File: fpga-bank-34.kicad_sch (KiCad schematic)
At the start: 5 parts, among them U1 XC7K410T-2FFG900I

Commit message: Bump revision to 1.0.0. Update name on schematic and PCB sheets
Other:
- title: K410T devboard -> Kintex 410T devboard

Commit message: Updated libraries for 100nF cap
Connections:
- net +0V675_VREF: now also C375.1
- net GND: now also C375.2
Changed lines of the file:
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@@
       (effects (font (size 1.27 1.27)) (justify left))
     )
+    (pin "1")
+    (pin "2")
   )
   (symbol (lib_id "K410T-devboard:C_100n_0402_EIA") (at 171.45 118.745 0) (unit 1)

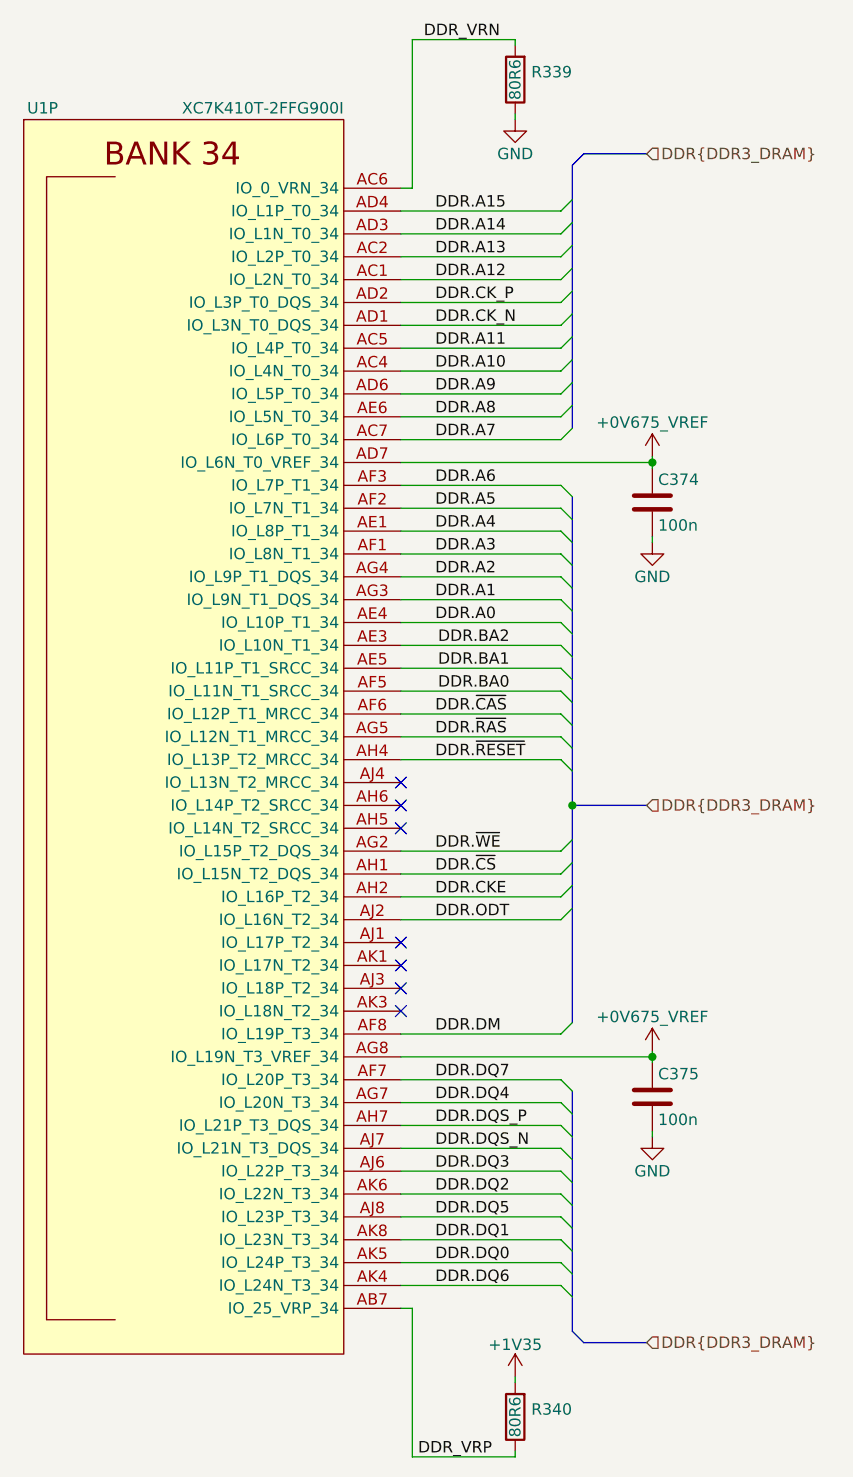
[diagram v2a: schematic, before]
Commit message: Introduce component standardization
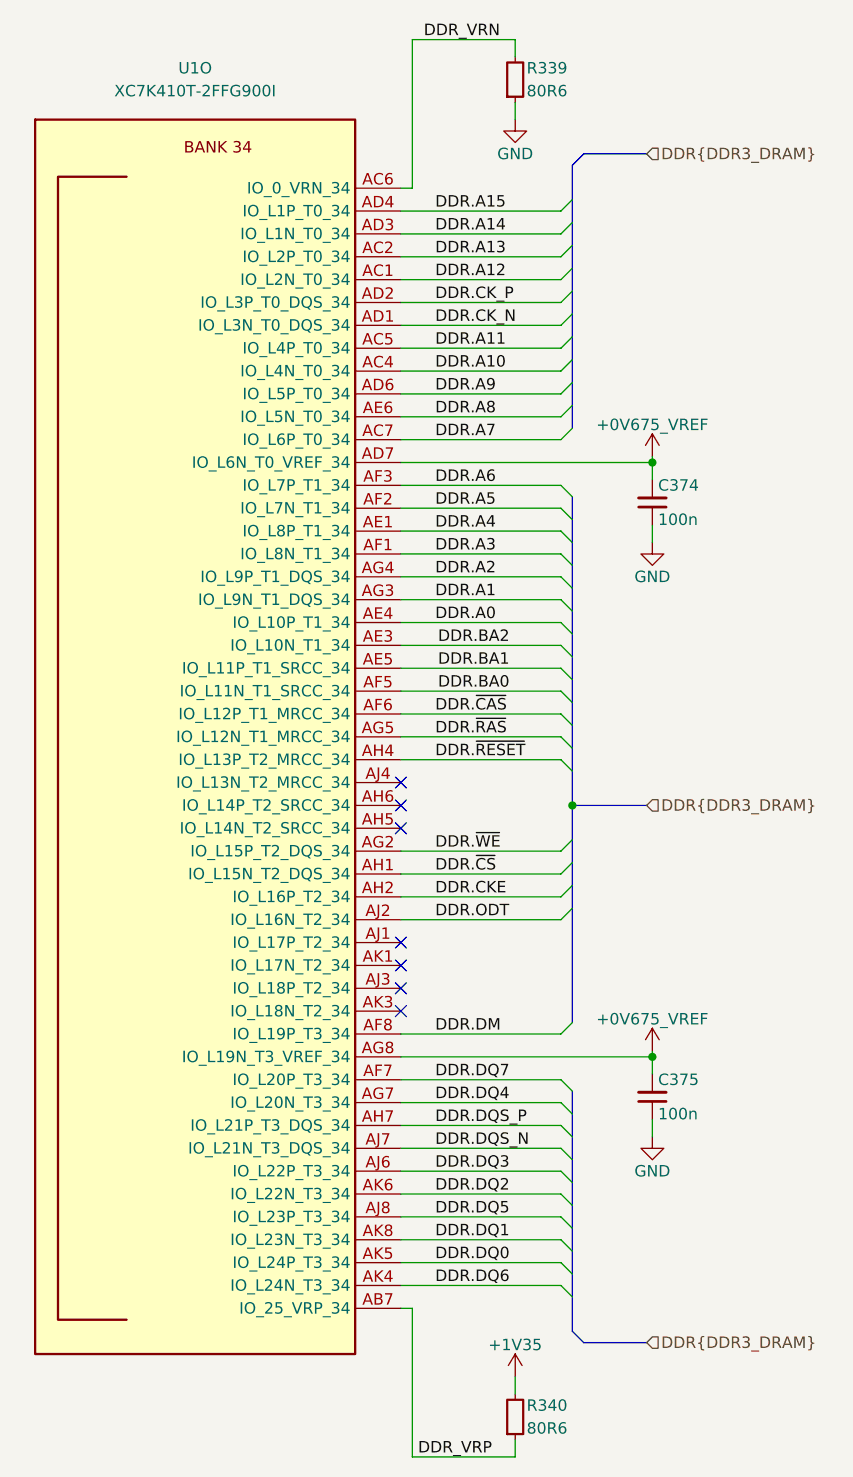
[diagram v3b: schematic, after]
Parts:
- removed U1: XC7K410T-2FFG900I, K410T-devboard-footprints:xc7k410t-2ffg900I, symbol K410T-devboard:XC7K410T-2FFG900I
- added U1: XC7K410T-2FFG900I, K410T-devboard-footprints:xc7k410t-2ffg900I, symbol K410T-devboard:XC7K410T-2FFG900I
- C374, C375: footprint K410T-devboard-footprints:0402-cap_EIA -> K410T-devboard-footprints:C_0402_1005Metric_EIA; Author (none) -> Antmicro; License (none) -> Apache-2.0
- R339, R340: footprint K410T-devboard-footprints:0402-res_EIA -> K410T-devboard-footprints:R_0402_1005Metric_EIA; Author (none) -> Antmicro; License (none) -> Apache-2.0; MPN MC00625W0402180R6 -> CR0402-FX-80R6GLF; Manufacturer MULTICOMP -> Bourns; Tolerance (none) -> 1%
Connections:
- net +0V675_VREF: now also C374.2, C375.2, U1.AD7 (IO_L6N_T0_VREF_34), U1.AG8 (IO_L19N_T3_VREF_34); no longer C374.1, C375.1
- net DDR.A0: now also U1.AE4 (IO_L10P_T1_34)
- net DDR.A1: now also U1.AG3 (IO_L9N_T1_DQS_34)
- net DDR.A10: now also U1.AC4 (IO_L4N_T0_34)
- net DDR.A11: now also U1.AC5 (IO_L4P_T0_34)
- net DDR.A12: now also U1.AC1 (IO_L2N_T0_34)
- net DDR.A13: now also U1.AC2 (IO_L2P_T0_34)
- net DDR.A14: now also U1.AD3 (IO_L1N_T0_34)
- net DDR.A15: now also U1.AD4 (IO_L1P_T0_34)
- net DDR.A2: now also U1.AG4 (IO_L9P_T1_DQS_34)
- net DDR.A3: now also U1.AF1 (IO_L8N_T1_34)
- net DDR.A4: now also U1.AE1 (IO_L8P_T1_34)
- net DDR.A5: now also U1.AF2 (IO_L7N_T1_34)
- net DDR.A6: now also U1.AF3 (IO_L7P_T1_34)
- net DDR.A7: now also U1.AC7 (IO_L6P_T0_34)
- net DDR.A8: now also U1.AE6 (IO_L5N_T0_34)
- net DDR.A9: now also U1.AD6 (IO_L5P_T0_34)
- net DDR.BA0: now also U1.AF5 (IO_L11N_T1_SRCC_34)
- net DDR.BA1: now also U1.AE5 (IO_L11P_T1_SRCC_34)
- net DDR.BA2: now also U1.AE3 (IO_L10N_T1_34)
- net DDR.CKE: now also U1.AH2 (IO_L16P_T2_34)
- net DDR.CK_N: now also U1.AD1 (IO_L3N_T0_DQS_34)
- net DDR.CK_P: now also U1.AD2 (IO_L3P_T0_DQS_34)
- net DDR.DM: now also U1.AF8 (IO_L19P_T3_34)
- net DDR.DQ0: now also U1.AK5 (IO_L24P_T3_34)
- net DDR.DQ1: now also U1.AK8 (IO_L23N_T3_34)
- net DDR.DQ2: now also U1.AK6 (IO_L22N_T3_34)
- net DDR.DQ3: now also U1.AJ6 (IO_L22P_T3_34)
- net DDR.DQ4: now also U1.AG7 (IO_L20N_T3_34)
- net DDR.DQ5: now also U1.AJ8 (IO_L23P_T3_34)
- net DDR.DQ6: now also U1.AK4 (IO_L24N_T3_34)
- net DDR.DQ7: now also U1.AF7 (IO_L20P_T3_34)
- net DDR.DQS_N: now also U1.AJ7 (IO_L21N_T3_DQS_34)
- net DDR.DQS_P: now also U1.AH7 (IO_L21P_T3_DQS_34)
- net DDR.ODT: now also U1.AJ2 (IO_L16N_T2_34)
- net DDR.~{CAS}: now also U1.AF6 (IO_L12P_T1_MRCC_34)
- net DDR.~{CS}: now also U1.AH1 (IO_L15N_T2_DQS_34)
- net DDR.~{RAS}: now also U1.AG5 (IO_L12N_T1_MRCC_34)
- net DDR.~{RESET}: now also U1.AH4 (IO_L13P_T2_MRCC_34)
- net DDR.~{WE}: now also U1.AG2 (IO_L15P_T2_DQS_34)
- net DDR_VRN: now also U1.AC6 (IO_0_VRN_34)
- net DDR_VRP: now also U1.AB7 (IO_25_VRP_34)
- net GND: now also C374.1, C375.1; no longer C374.2, C375.2
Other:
- moved on the sheet: C374, C375

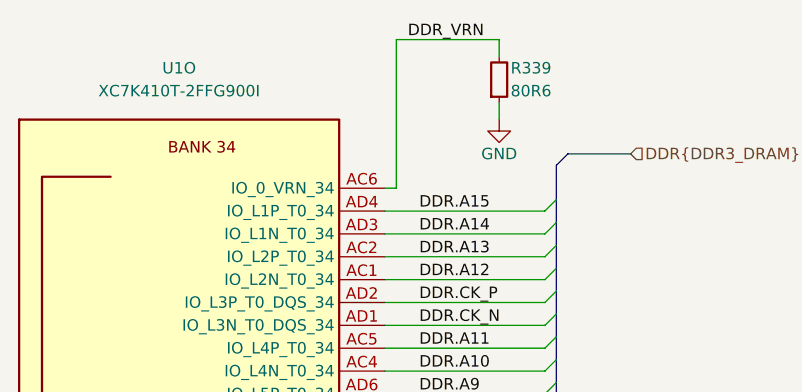
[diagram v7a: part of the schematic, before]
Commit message: [#55729] Change Manufacturer to AMD-Xilinx
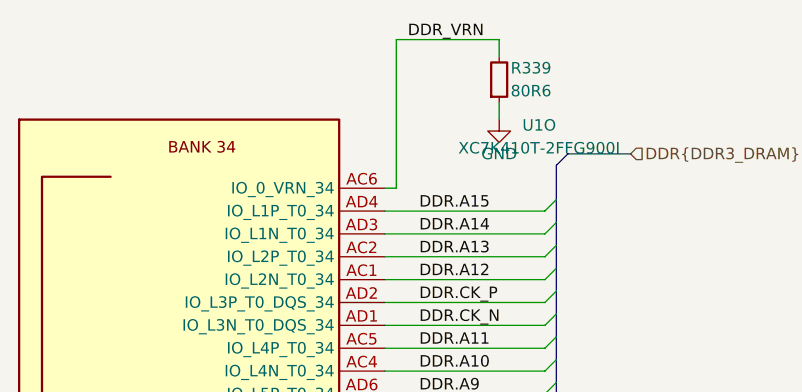
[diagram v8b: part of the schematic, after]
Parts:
- U1: Manufacturer Xilinx -> AMD-Xilinx
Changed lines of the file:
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@@
   (symbol (lib_id "K410T-devboard:XC7K410T-2FFG900I") (at 143.51 83.82 0) (unit 15)
     (in_bom yes) (on_board yes) (dnp no) (fields_autoplaced)
-    (property "Reference" "U1" (at 120.65 70.485 0)
+    (property "Reference" "U1" (at 160.655 76.835 0)
       (effects (font (size 1.27 1.27) (thickness 0.15)))
     )
-    (property "Value" "XC7K410T-2FFG900I" (at 120.65 73.025 0)
+    (property "Value" "XC7K410T-2FFG900I" (at 160.655 79.375 0)
       (effects (font (size 1.27 1.27) (thickness 0.15)))
     )
@@
       (effects (font (size 1.27 1.27) (thickness 0.15)) (justify left bottom) hide)
     )
-    (property "Manufacturer" "Xilinx" (at 143.51 62.23 0)
+    (property "Manufacturer" "AMD-Xilinx" (at 143.51 62.23 0)
       (effects (font (size 1.27 1.27) (thickness 0.15)) (justify left bottom) hide)
     )
@@
           (reference "U1") (unit 15)
         )
+        (path "/c1489e7c-896d-4046-acd4-3929998e87dc/020031b8-7f27-4e26-b74c-26be7f0881a9"
+          (reference "U1") (unit 15)
+        )
